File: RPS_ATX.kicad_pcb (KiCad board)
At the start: 2 copper layers, 100 x 50 mm, 104 parts, among them J1 Fan_in, J10 DISP, J11 ENC1, J12 ENC2, J13 Fan_out, J14 TEMP_SEN, J2 C1, J3 C2, J4 17.5V, J5 PS_OUT-, J6 PS_OUT+, J7 RPS_OUT+, J8 SWD, J9 RPS_OUT-, Q1 AO3400A, Q2 AO3400A, Q3 AO3400A, U1 TL494, U2 AMS1117-3.3, U3 L7815, U5 INA180A2, U6 ICL7660A, U7 LM7805_TO220, U8 STM32G431RBT6, U9 OP07, Y1 8MHz

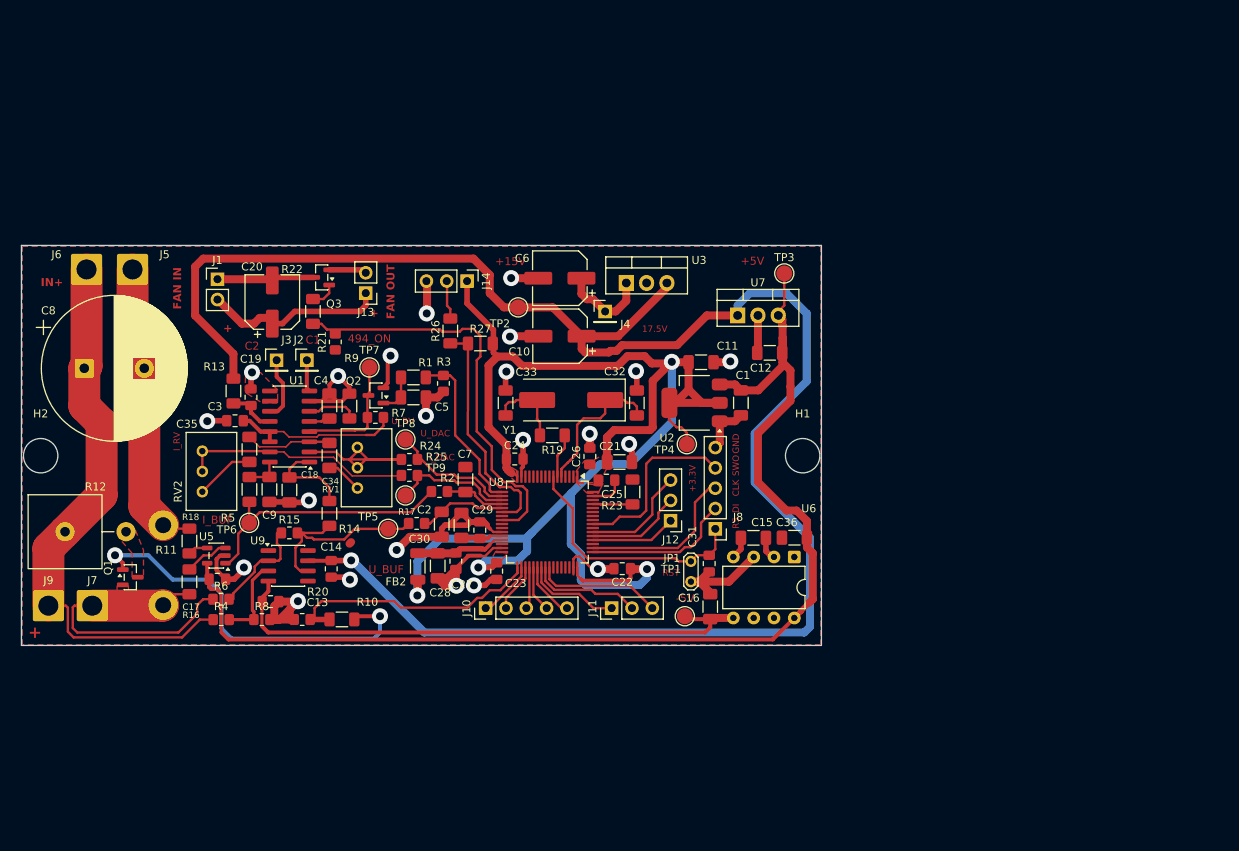
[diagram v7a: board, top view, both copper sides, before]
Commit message: excluding STM32G431
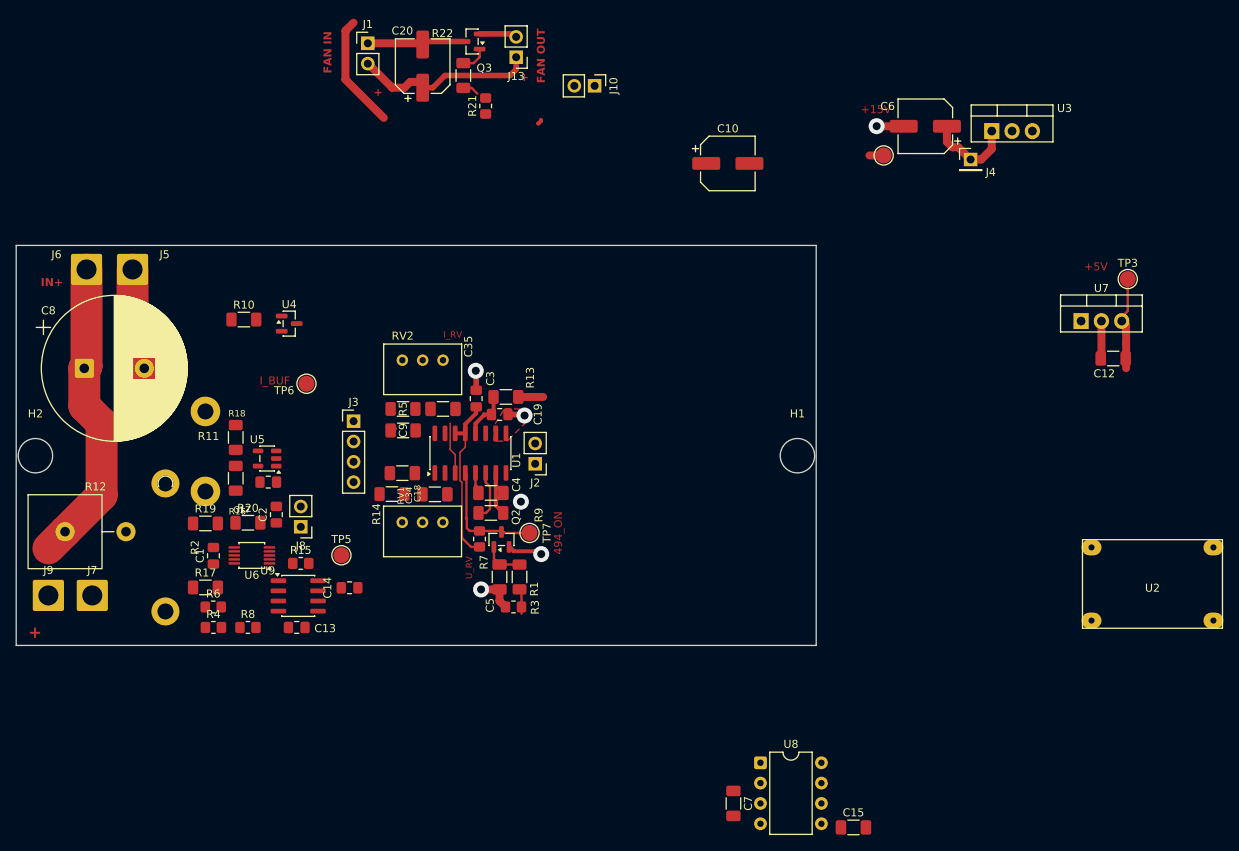
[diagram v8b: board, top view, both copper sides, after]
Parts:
- removed C11, C16, C21, C36: 10u, Capacitor_SMD:C_1206_3216Metric_Pad1.33x1.80mm_HandSolder
- removed C22, C23, C24, C25, C26, C27, C29, C31: 100n, Capacitor_SMD:C_0805_2012Metric_Pad1.18x1.45mm_HandSolder
- removed C28, C30: 1u, Capacitor_SMD:C_1206_3216Metric_Pad1.33x1.80mm_HandSolder
- removed C32, C33: 20p, Capacitor_SMD:C_1206_3216Metric_Pad1.33x1.80mm_HandSolder
- removed FB2: FB, Inductor_SMD:L_1206_3216Metric_Pad1.22x1.90mm_HandSolder
- removed J11: ENC1, Connector_PinHeader_2.54mm:PinHeader_1x03_P2.54mm_Vertical
- removed J12: ENC2, Connector_PinHeader_2.54mm:PinHeader_1x03_P2.54mm_Vertical
- removed J14: TEMP_SEN, Connector_PinHeader_2.54mm:PinHeader_1x03_P2.54mm_Vertical
- removed JP1: RST, TestPoint:TestPoint_2Pads_Pitch2.54mm_Drill0.8mm
- removed Q1: AO3400A, Package_TO_SOT_SMD:SOT-23
- removed R23: 10K, Resistor_SMD:R_1206_3216Metric_Pad1.30x1.75mm_HandSolder
- removed R24, R25: 5.1K, Resistor_SMD:R_0805_2012Metric_Pad1.20x1.40mm_HandSolder
- removed R26, R27: 470R, Resistor_SMD:R_1206_3216Metric_Pad1.30x1.75mm_HandSolder
- removed TP1: -5V, TestPoint:TestPoint_Pad_D2.0mm
- removed TP4: +3.3V, TestPoint:TestPoint_Pad_D2.0mm
- removed TP8: U_DAC, TestPoint:TestPoint_Pad_D2.0mm
- removed TP9: I_DAC, TestPoint:TestPoint_Pad_D2.0mm
- removed Y1: 8MHz, Crystal:Crystal_SMD_HC49-SD
- added U4: TL431DBZ, Package_TO_SOT_SMD:SOT-23, F.Cu at (88.5, 65.0)
- C1: value 10u -> 100n; footprint Capacitor_SMD:C_1206_3216Metric_Pad1.33x1.80mm_HandSolder -> Capacitor_SMD:C_0805_2012Metric_Pad1.18x1.45mm_HandSolder
- C2: value 1u -> 100n; footprint Capacitor_SMD:C_1206_3216Metric_Pad1.33x1.80mm_HandSolder -> Capacitor_SMD:C_0805_2012Metric_Pad1.18x1.45mm_HandSolder
- C7: value 1u -> 10u
- J10: value DISP -> CTRL; footprint Connector_PinHeader_2.54mm:PinHeader_1x05_P2.54mm_Vertical -> Connector_PinHeader_2.54mm:PinHeader_1x02_P2.54mm_Vertical
- J2: value C1 -> 494_OUT; footprint Connector_PinHeader_2.54mm:PinHeader_1x01_P2.54mm_Vertical -> Connector_PinHeader_2.54mm:PinHeader_1x02_P2.54mm_Vertical
- J3: value C2 -> POT; footprint Connector_PinHeader_2.54mm:PinHeader_1x01_P2.54mm_Vertical -> Connector_PinHeader_2.54mm:PinHeader_1x04_P2.54mm_Vertical
- J7: value RPS_OUT+ -> RPS_OUT-
- J8: value SWD -> MEAS; footprint Connector_PinHeader_2.54mm:PinHeader_1x05_P2.54mm_Vertical -> Connector_PinHeader_2.54mm:PinHeader_1x02_P2.54mm_Vertical
- J9: value RPS_OUT- -> RPS_OUT+
- R10: value 100R -> 1K
- R17, R20: value 5.1K -> 10R; footprint Resistor_SMD:R_0805_2012Metric_Pad1.20x1.40mm_HandSolder -> Resistor_SMD:R_1206_3216Metric_Pad1.30x1.75mm_HandSolder
- R19: value 0R -> 10R
- R2: value 5.1K -> 0.005R; footprint Resistor_SMD:R_0805_2012Metric_Pad1.20x1.40mm_HandSolder -> MyLibrary:Shunt 0.005R
- U2: value AMS1117-3.3 -> Mini360; footprint Package_TO_SOT_SMD:SOT-223-3_TabPin2 -> Mini360_step-down:Mini360_step-down
- U6: value ICL7660A -> INA226; footprint Package_DIP:DIP-8_W7.62mm -> Package_SO:VSSOP-10_3x3mm_P0.5mm
- U8: value STM32G431RBT6 -> ICL7660; footprint Package_QFP:LQFP-64_10x10mm_P0.5mm -> Package_DIP:DIP-8_W7.62mm
- moved C1 68.6 mm to (79.0, 94.0), turned to 90 degrees
- moved U6 67.8 mm to (83.8, 94.0), turned to 180 degrees
- moved J10 66.7 mm to (126.7, 35.3), turned to -90 degrees
- moved U2 61.6 mm to (196.4, 97.6), turned to 0 degrees
- moved C7 52.5 mm to (144.0, 125.0), turned to -90 degrees
- moved J8 51.8 mm to (89.9, 90.4)
- moved J4 49.5 mm to (173.6, 44.5)
- moved TP2 49.5 mm to (162.8, 44.0)
- moved U3 49.5 mm to (176.3, 41.0)
- moved C6 49.5 mm to (168.0, 40.4)
- moved R19 44.7 mm to (78.0, 90.0), turned to 0 degrees
- moved C12 42.9 mm to (191.5, 69.4)
- moved TP3 42.9 mm to (193.3, 59.5)
- moved U7 42.9 mm to (187.5, 64.7)
- moved U8 40.2 mm to (147.4, 119.9), turned to 0 degrees
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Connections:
- net C1 renamed Net-(J2-Pin_1)
- C1 pad 1: +5V -> Net-(U6-Vin+)
- C1 pad 2: GND -> Net-(U6-Vin-)
- C15 pad 1: Net-(U6-CAP+) -> -5V
- C15 pad 2: Net-(U6-CAP-) -> GND
- C2 pad 1: MCU_ADC_U -> +5V
- C7 pad 1: MCU_ADC_I -> Net-(U8-CAP+)
- C7 pad 2: GND -> Net-(U8-CAP-)
- J10 pad 1: DISP_DC -> MCU_494_ON
- J10 pad 2: DISP_SCK -> MCU_FAN
- J3 pad 1: C2 -> GND
- J7 pad 1: MEAS_I+ -> Net-(J7-Pin_1)
- J8 pad 1: MCU_RST -> Net-(J8-Pin_1)
- J8 pad 2: MCU_SWDIO -> Net-(J8-Pin_2)
- R10 pad 1: MCU_DCH -> +5V_REF
- R10 pad 2: Net-(Q1-G) -> +2V5
- R12 pad 2: Net-(Q1-D) -> MEAS_I+
- R13 pad 1: +15V -> +17.5V_ATX
- R17 pad 1: Net-(R14-Pad1) -> Net-(J7-Pin_1)
- R17 pad 2: MCU_ADC_U -> Net-(U6-Vin+)
- R19 pad 1: MCU_OSC_OUT -> MEAS_I+
- R19 pad 2: Net-(C33-Pad1) -> Net-(U6-Vin-)
- R2 pad 1: /Analog/i_op_out -> MEAS_I+
- R2 pad 2: MCU_ADC_I -> Net-(J7-Pin_1)
- R20 pad 1: GND -> Net-(U6-VS)
- R20 pad 2: MCU_DCH -> +5V
- U1 pad 11: C2 -> Net-(J2-Pin_2)
- U2 pad 2: +3.3V -> +17.5V_ATX
- U2 pad 3: +5V -> GND
- U6 pad 1: unconnected-(U6-NC-Pad1) -> GND
- U6 pad 2: Net-(U6-CAP+) -> GND
- U6 pad 3: GND -> unconnected-(U6-~{Alert}-Pad3)
- U6 pad 4: Net-(U6-CAP-) -> Net-(J8-Pin_1)
- U6 pad 5: -5V -> Net-(J8-Pin_2)
- U6 pad 6: unconnected-(U6-LV-Pad6) -> Net-(U6-VS)
- U6 pad 7: unconnected-(U6-OSC-Pad7) -> GND
- U6 pad 8: +5V -> VOUT
- U7 pad 1: +15V -> +8V
- U8 pad 1: +3.3V -> unconnected-(U8-NC-Pad1)
- U8 pad 2: unconnected-(U8-PC13-Pad2) -> Net-(U8-CAP+)
- U8 pad 3: unconnected-(U8-PC14-Pad3) -> GND
- U8 pad 4: unconnected-(U8-PC15-Pad4) -> Net-(U8-CAP-)
- U8 pad 5: MCU_OSC_IN -> -5V
- U8 pad 6: MCU_OSC_OUT -> unconnected-(U8-LV-Pad6)
- U8 pad 7: MCU_RST -> unconnected-(U8-OSC-Pad7)
- U8 pad 8: unconnected-(U8-PC0-Pad8) -> +5V
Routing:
- net +15V: track 230.6 -> 16.6 mm, vias 1 -> 0
- net +3.3V: track 194.8 -> 0.00 mm, vias 4 -> 0
- net GND: track 200.3 -> 46.8 mm, vias 22 -> 6
- net +5V: track 146.1 -> 12.0 mm
- net -5V: track 69.4 -> 0.00 mm
- net MCU_FAN: track 51.2 -> 2.05 mm
- net Net-(Q1-G): track 47.9 -> 0.00 mm, vias 2 -> 0
- net MEAS_I+: track 37.4 -> 0.65 mm
- net /Analog/i_op_out: track 33.6 -> 0.49 mm
- net MCU_DCH: track 31.8 -> 0.00 mm
- net MCU_RST: track 31.6 -> 0.00 mm
- net VOUT: track 70.2 -> 38.6 mm
- net MCU_TEMP: track 29.1 -> 0.00 mm
- net I_2IN-: track 28.7 -> 0.14 mm
- net U_1IN-: track 27.5 -> 0.00 mm
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- removed copper zone on F.Cu, net +3.3V
- removed copper zone on B.Cu, net GND
- removed copper zone on F.Cu, net MEAS_I+
- removed copper zone on F.Cu, net Net-(Q1-D)
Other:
- board text removed: "CLK"
- board text removed: "DI"
- board text removed: "GND"
- board text removed: "RS"
- board text removed: "SWO"
